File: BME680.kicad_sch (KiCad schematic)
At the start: 20 parts, among them IC1 BME680, Q2 BSS138, U2 AP2112K-3.3

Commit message: added drawing sheet
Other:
- title: (none) -> BME680
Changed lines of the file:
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@@
 	(generator "eeschema")
 	(generator_version "8.0")
-	(paper "User" 383.616 217.322)
+	(paper "A4")
+	(title_block
+		(title "BME680")
+		(date "2024-03-06")
+	)
 	(junction
 		(at 175.26 55.88)
@@
 					(unit 1)
 				)
-			)
-		)
-	)
-	(symbol
-		(lib_id "BME680-eagle-import:FRAME_A4_ADAFRUIT")
-		(at 17.78 198.12 0)
-		(unit 1)
-		(exclude_from_sim no)
-		(in_bom yes)
-		(on_board yes)
-		(dnp no)
-		(property "Reference" "#U$18"
-			(at 17.78 198.12 0)
-			(effects
-				(font
-					(size 1.27 1.27)
-				)
-				(hide yes)
-			)
-		)
-		(property "Value" "FRAME_A4_ADAFRUIT"
-			(at 17.78 198.12 0)
-			(effects
-				(font
-					(size 1.27 1.27)
-				)
-				(hide yes)
-			)
-		)
-		(property "Footprint" ""
-			(at 17.78 198.12 0)
-			(effects
-				(font
-					(size 1.27 1.27)
-				)
-				(hide yes)
-			)
-		)
-		(property "Datasheet" ""
-			(at 17.78 198.12 0)
-			(effects
-				(font
-					(size 1.27 1.27)
-				)
-				(hide yes)
-			)
-		)
-		(property "Description" ""
-			(at 17.78 198.12 0)
-			(effects
-				(font
-					(size 1.27 1.27)
-				)
-				(hide yes)
-			)
-		)
-		(instances
-			(project "BME680"
-				(path "/ba694707-55c1-41d4-b2e7-4006a8fc6a7f"
-					(reference "#U$18")
-					(unit 1)
-				)

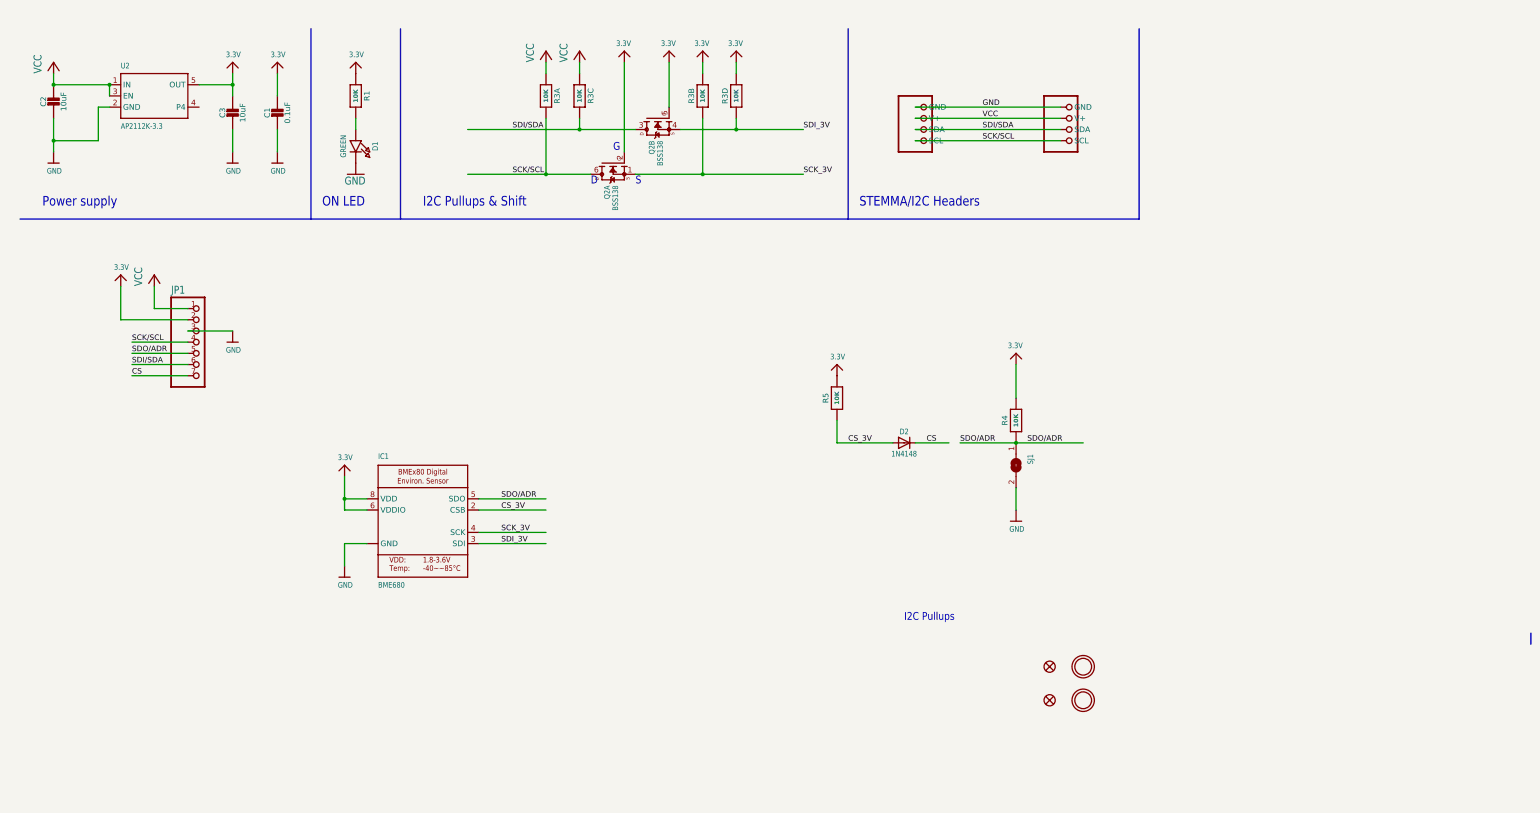
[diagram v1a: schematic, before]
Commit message: update BME680 scheme
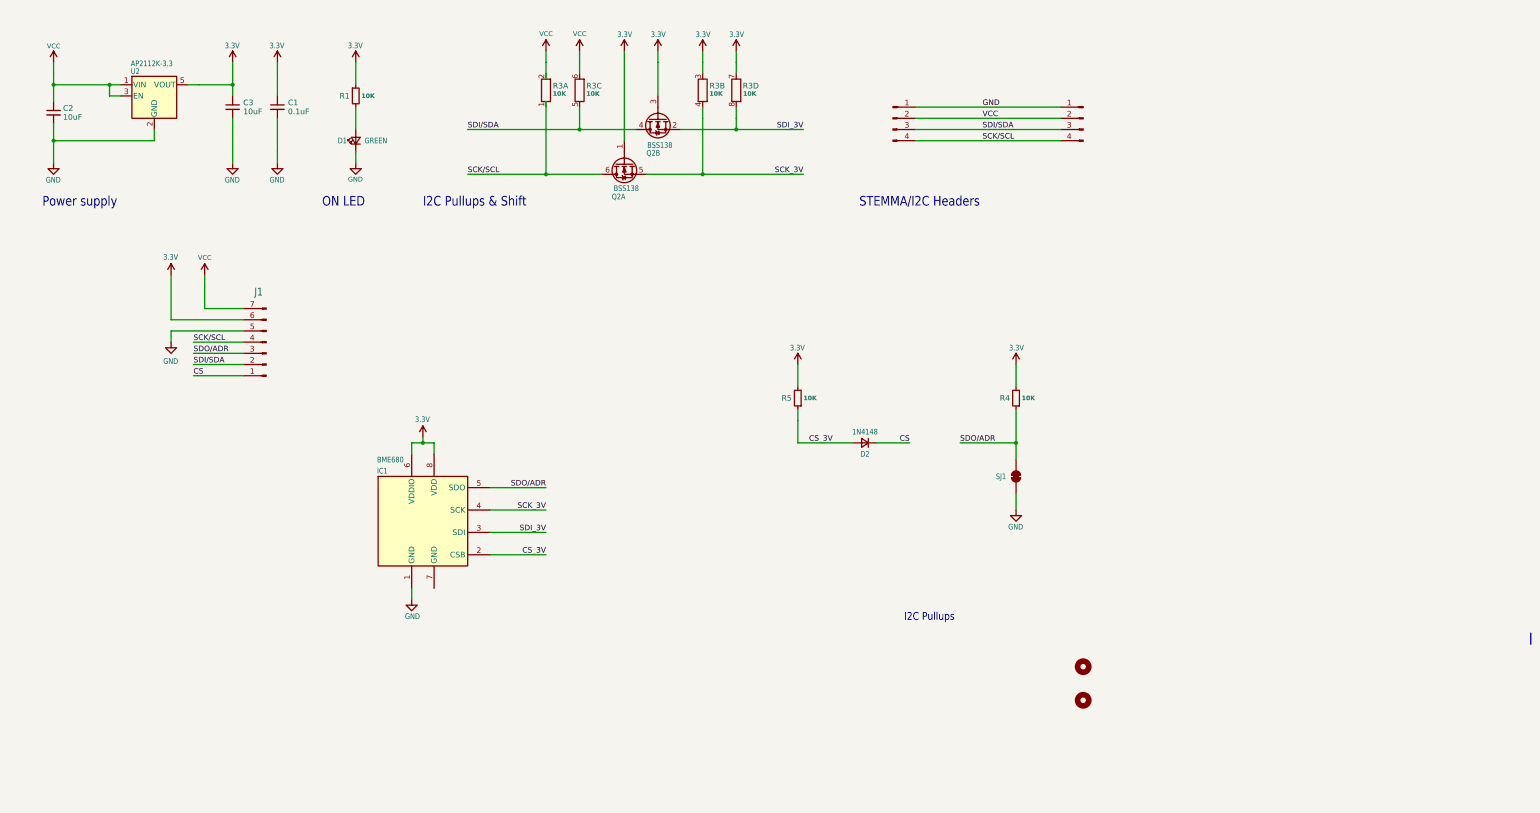
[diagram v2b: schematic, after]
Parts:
- removed FID3, FID4: FIDUCIAL_1MM, BME680:FIDUCIAL_1MM, symbol BME680-eagle-import:FIDUCIAL_1MM
- C1: footprint BME680:0603-NO -> Capacitor_SMD:C_0603_1608Metric; symbol BME680-eagle-import:CAP_CERAMIC0603_NO -> Device:C_Small
- C2, C3: footprint BME680:0805-NO -> Capacitor_SMD:C_0805_2012Metric; symbol BME680-eagle-import:CAP_CERAMIC0805-NOOUTLINE -> Device:C_Small
- CONN3, CONN4: footprint BME680:JST_SH4 -> Connector_JST:JST_SH_SM04B-SRSS-TB_1x04-1MP_P1.00mm_Horizontal; symbol BME680-eagle-import:STEMMA_I2C_QT -> Connector:Conn_01x04_Pin
- D1: footprint BME680:CHIPLED_0603_NOOUTLINE -> LED_SMD:LED_0603_1608Metric; symbol BME680-eagle-import:LED0603_NOOUTLINE -> Device:LED_Small
- D2: footprint BME680:SOD-323 -> Diode_SMD:D_SOD-323; symbol BME680-eagle-import:DIODESOD-323 -> Device:D_Small
- IC1: footprint BME680:BME680 -> Package_LGA:Bosch_LGA-8_3x3mm_P0.8mm_ClockwisePinNumbering; symbol BME680-eagle-import:BME680 -> Sensor:BME680
- J1: renamed from JP1; footprint BME680:1X07_ROUND_70 -> Connector_PinHeader_2.54mm:PinHeader_1x07_P2.54mm_Vertical; symbol BME680-eagle-import:HEADER-1X770MIL -> Connector:Conn_01x07_Pin
- Q2: footprint BME680:SOT363 -> Package_TO_SOT_SMD:SOT-363_SC-70-6; symbol BME680-eagle-import:MOSFET-N_DUAL -> Device:Q_Dual_NMOS_G1S2G2D2S1D1
- R1, R4, R5: footprint BME680:0603-NO -> Resistor_SMD:R_0603_1608Metric; symbol BME680-eagle-import:RESISTOR_0603_NOOUT -> Device:R_Small
- R3: footprint BME680:RESPACK_4X0603 -> Resistor_THT:R_Array_SIP8; symbol BME680-eagle-import:RESISTOR_4PACK -> Device:R_Pack04_SIP_Split
- SJ1: footprint BME680:SOLDERJUMPER_ARROW_NOPASTE -> Jumper:SolderJumper-2_P1.3mm_Open_TrianglePad1.0x1.5mm; symbol BME680-eagle-import:SOLDERJUMPER -> Jumper:SolderJumper_2_Bridged; now left out of the parts list
- U$1, U$17: footprint BME680:MOUNTINGHOLE_2.5_PLATED -> MountingHole:MountingHole_2.5mm; symbol BME680-eagle-import:MOUNTINGHOLE2.5 -> Mechanical:MountingHole; now left out of the parts list
- U2: footprint BME680:SOT23-5 -> Package_TO_SOT_SMD:SOT-23-5; symbol BME680-eagle-import:VREG_SOT23-5 -> Regulator_Linear:AP2112K-3.3
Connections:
- net 3.3V: now also J1.6 (Pin_6), Q2.1 (G), Q2.3 (G), R3.3 (R2.1), R3.7 (R4.1); no longer J1.2, Q2.2 (G), Q2.5 (G), R3.2 (1), R3.4 (1)
- net CS: now also D2.1 (K), J1.1 (Pin_1); no longer D2.C, J1.7
- net CS_3V: now also D2.2 (A); no longer D2.A
- net GND: now also D1.1 (K), J1.5 (Pin_5); no longer D1.C, IC1.7 (GND), J1.3
- net SCK/SCL: no longer R3.8 (2)
- net SCK_3V: now also Q2.5 (S), R3.4 (R2.2); no longer Q2.1 (S), R3.7 (2)
- net SDI/SDA: now also J1.2 (Pin_2), Q2.4 (D), R3.5 (R3.1); no longer J1.6, Q2.3 (D), R3.6 (2)
- net SDI_3V: now also Q2.2 (S), R3.8 (R4.2); no longer Q2.4 (S), R3.5 (2)
- net SDO/ADR: now also J1.3 (Pin_3); no longer J1.5
- net VCC: now also J1.7 (Pin_7), R3.2 (R1.2), R3.6 (R3.2); no longer J1.1, R3.1, R3.3 (1)
- net at R1.2: now also D1.2 (A); no longer D1.A
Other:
- note removed: "D"
- note removed: "G"
- note removed: "S"

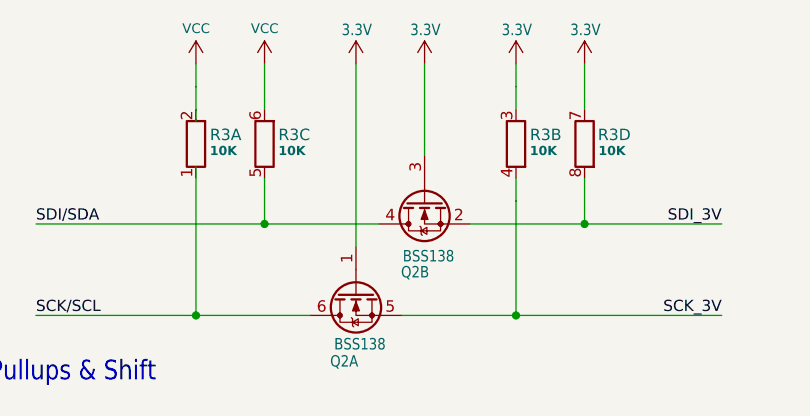
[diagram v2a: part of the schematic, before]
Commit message: update BME680 routing and footprints
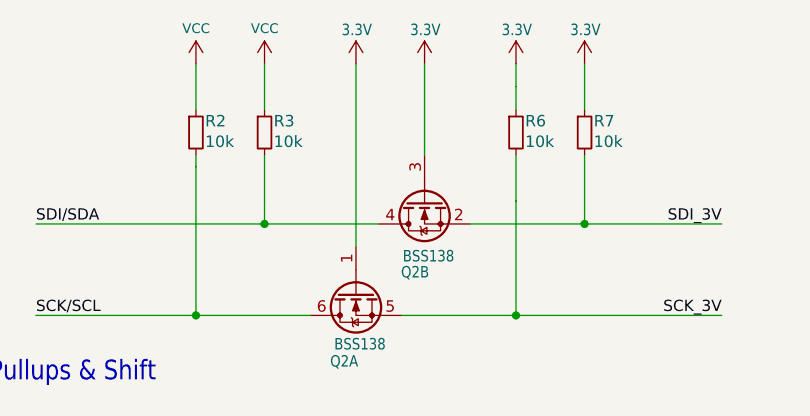
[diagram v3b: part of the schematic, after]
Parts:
- removed R3: 10K, Resistor_THT:R_Array_SIP8, symbol Device:R_Pack04_SIP_Split
- added R2, R3, R6, R7: 10k, Resistor_SMD:R_0603_1608Metric, symbol Device:R_Small
- D1: Componant package type (none) -> LED_0603; MPN (none) -> 150060GS75000; Manufacturer (none) -> Würth Elektronik; SPN (none) -> 732-4971-2-ND; Supplier (none) -> DigiKey
- D2: Componant package type (none) -> SOD-323; MPN (none) -> 1N4148WX-TP; Manufacturer (none) -> Micro Commercial Co; SPN (none) -> 1N4148WXTPMSTR-ND; Supplier (none) -> DigiKey
- IC1: Componant package type (none) -> /; MPN (none) -> BME680; Manufacturer (none) -> Bosch Sensortec; SPN (none) -> 828-1077-2-ND; Supplier (none) -> DigiKey
- Q2: Componant package type (none) -> SOT-363; MPN (none) -> BSS138DWQ-7; Manufacturer (none) -> Diodes Incorporated; SPN (none) -> BSS138DWQ-7DITR-ND; Supplier (none) -> DigiKey
- U2: Componant package type (none) -> SOT-25; MPN (none) -> AP2112K-3.3TRG1; Manufacturer (none) -> Diodes Incorporate; SPN (none) -> AP2112K-3.3TRG1DITR-ND; Supplier (none) -> DigiKey
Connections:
- net 3.3V: now also R6.1, R7.1
- net SCK/SCL: now also R2.2
- net SCK_3V: now also R6.2
- net SDI/SDA: now also R3.2
- net SDI_3V: now also R7.2
- net VCC: now also R2.1, R3.1

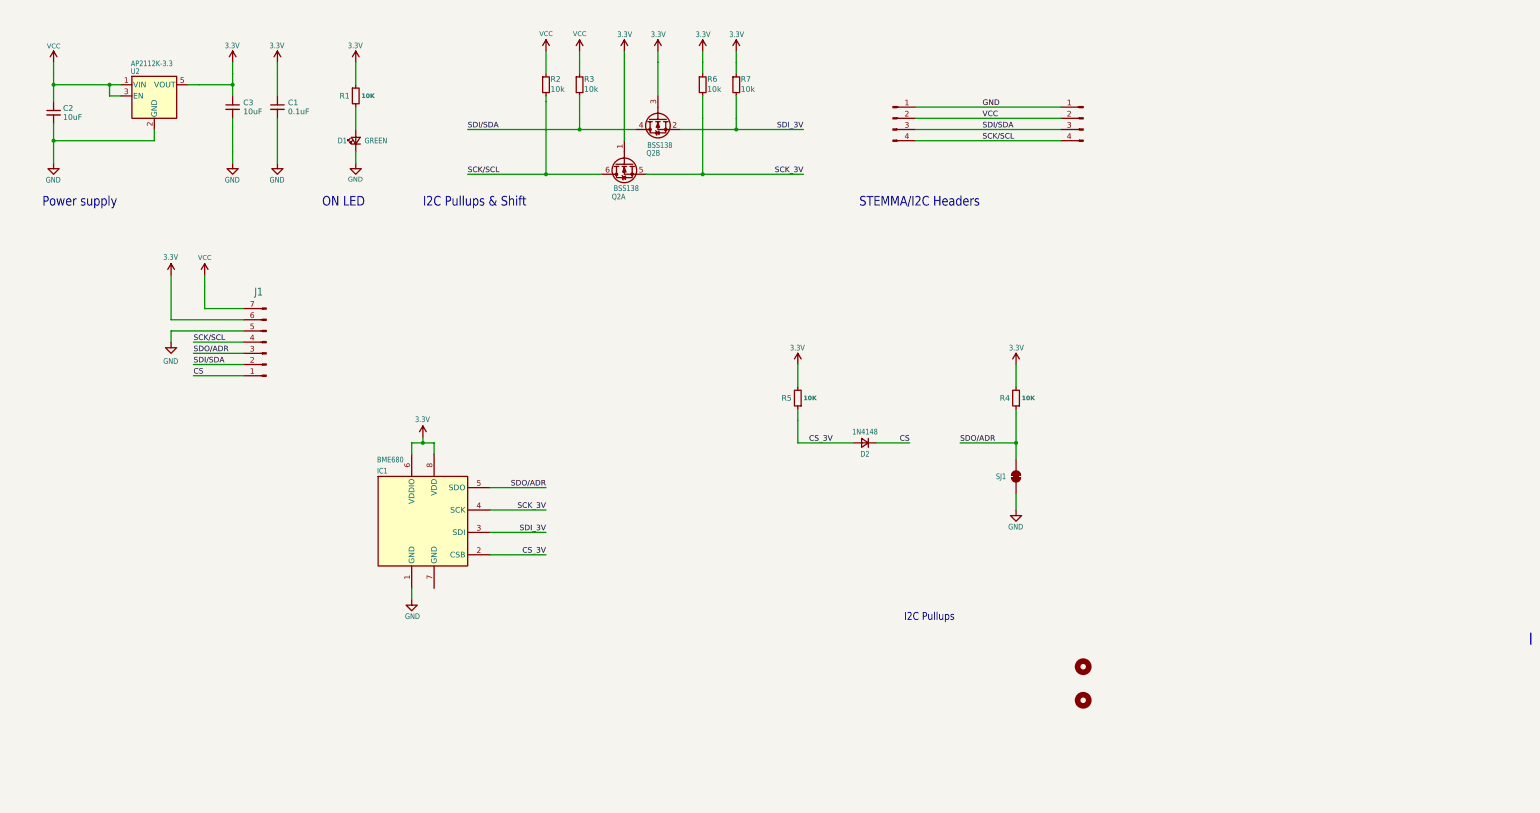
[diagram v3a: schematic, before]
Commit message: minor fixes in silkscreen and schematic layout
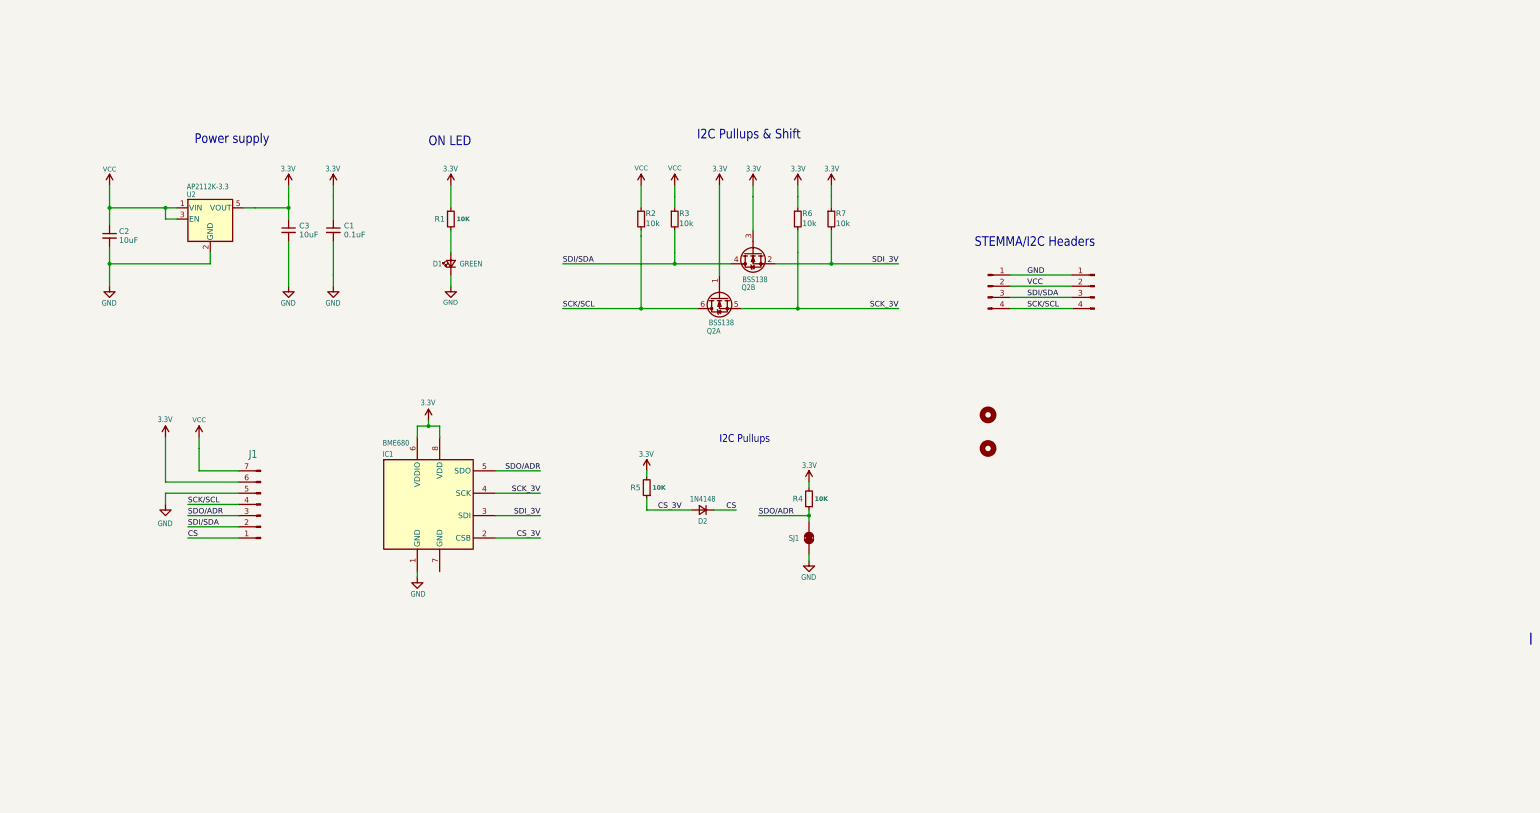
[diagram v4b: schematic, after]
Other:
- moved on the sheet: C1, C2, C3, D1, D2, IC1, J1, Q2A, Q2B, R1, R2, R3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

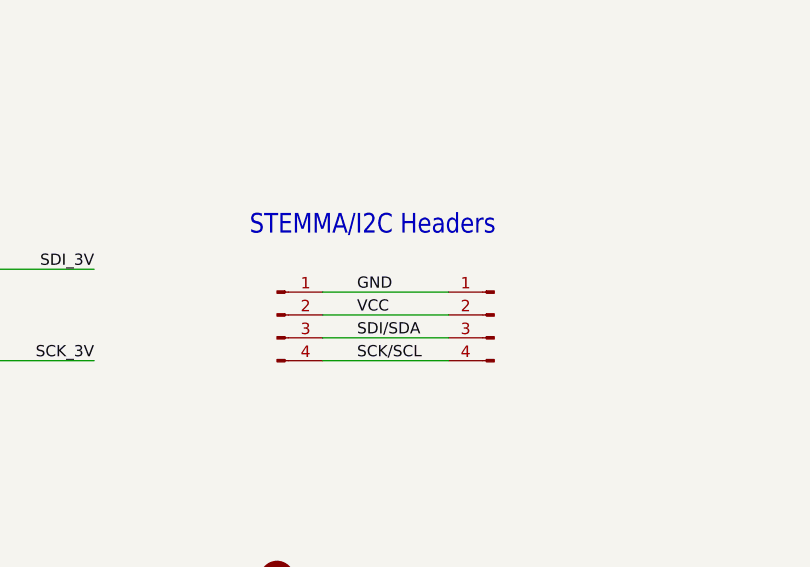
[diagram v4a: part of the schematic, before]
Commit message: routing done with freerouting + delete stemma connectors
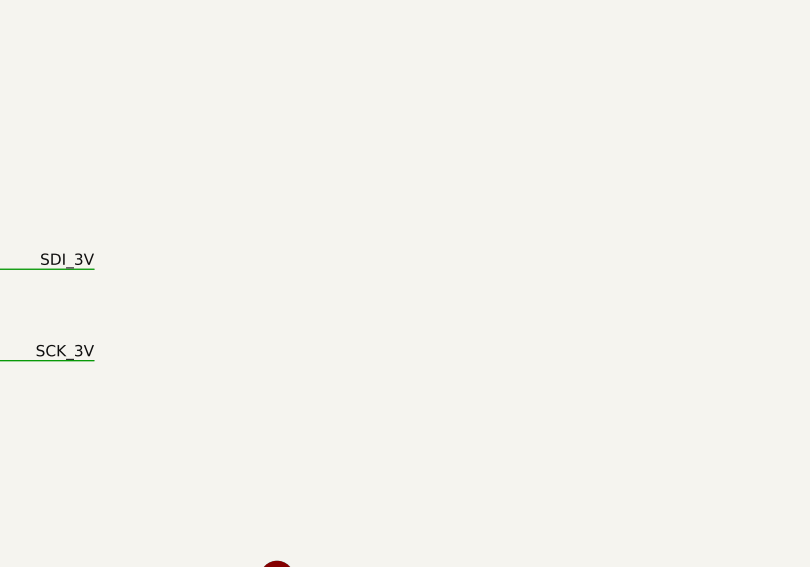
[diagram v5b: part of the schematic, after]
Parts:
- removed CONN3, CONN4: STEMMA_I2C_QT, Connector_JST:JST_SH_SM04B-SRSS-TB_1x04-1MP_P1.00mm_Horizontal, symbol Connector:Conn_01x04_Pin
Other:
- note removed: "STEMMA/I2C Headers"

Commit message: silkscreen update + BOM finalisation
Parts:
- C1: Componant package type (none) -> C_0603; MPN (none) -> /; Manufacturer (none) -> /; SPN (none) -> GPC0603104-100; Supplier (none) -> Eurocircuits
- C2, C3: Componant package type (none) -> C_0805; MPN (none) -> /; Manufacturer (none) -> /; SPN (none) -> GPC0805106-25; Supplier (none) -> Eurocircuits
- R1, R4, R5: value 10K -> 10k; Componant package type (none) -> R_0603; MPN (none) -> /; Manufacturer (none) -> /; SPN (none) -> GPR060310K; Supplier (none) -> Eurocircuits
- R2, R3, R6, R7: Componant package type (none) -> R_0603; MPN (none) -> /; Manufacturer (none) -> /; SPN (none) -> GPR060310K; Supplier (none) -> Eurocircuits
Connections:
- no-connect marks 0 -> 1

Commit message: BOM update
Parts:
- J1: Componant package type (none) -> /; MPN (none) -> TSW-107-23-G-S; Manufacturer (none) -> Samtec Inc.; SPN (none) -> SAM1069-07-ND; Supplier (none) -> DigiKey
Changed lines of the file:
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@@
 			)
 		)
-		(property "Description" "Generic connector, single row, 01x07, script generated"
+		(property "Description" "CONN HEADER VERT 7POS 2.54MM"
 			(at 74.93 130.81 0)
 			(effects
@@
 			)
 		)
-		(property "Componant package type" ""
+		(property "Componant package type" "/"
 			(at 74.93 130.81 0)
 			(effects
@@
 			)
 		)
-		(property "MPN" ""
+		(property "MPN" "TSW-107-23-G-S"
 			(at 74.93 130.81 0)
 			(effects
@@
 			)
 		)
-		(property "Manufacturer" ""
+		(property "Manufacturer" "Samtec Inc."
 			(at 74.93 130.81 0)
 			(effects
@@
 			)
 		)
-		(property "SPN" ""
+		(property "SPN" "SAM1069-07-ND"
 			(at 74.93 130.81 0)
 			(effects
@@
 			)
 		)
-		(property "Supplier" ""
+		(property "Supplier" "DigiKey"
 			(at 74.93 130.81 0)
 			(effects

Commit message: mosfet update
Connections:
- net 3.3V: now also Q2.2 (G), Q2.5 (G); no longer Q2.1 (G), Q2.3 (G)
- net SCK_3V: now also Q2.1 (S); no longer Q2.5 (S)
- net SDI/SDA: now also Q2.3 (D); no longer Q2.4 (D)
- net SDI_3V: now also Q2.4 (S); no longer Q2.2 (S)
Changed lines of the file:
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@@
 		(dnp no)
 		(property "Reference" "Q2"
-			(at 187.198 82.296 90)
+			(at 186.944 82.042 90)
 			(effects
 				(font
@@
 		)
 		(property "Value" "BSS138"
-			(at 189.992 80.518 90)
+			(at 189.992 80.137 90)
 			(effects
 				(font
@@
 	)
 	(symbol
+		(lib_name "Q_Dual_NMOS_G1S2G2D2S1D1_1")
 		(lib_id "Device:Q_Dual_NMOS_G1S2G2D2S1D1")
 		(at 179.07 83.82 90)
